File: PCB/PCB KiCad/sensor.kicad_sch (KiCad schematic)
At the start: 0 parts

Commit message: draw schematic for 60%
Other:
- note added: "TO DO: Complete analog front"
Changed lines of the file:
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@@
 (kicad_sch (version 20211123) (generator eeschema)
   (paper "A4")
+  (text "TO DO:\nComplete analog front" (at 118.11 80.01 0)
+    (effects (font (size 1.5 1.5)) (justify left bottom))
+  )
 )

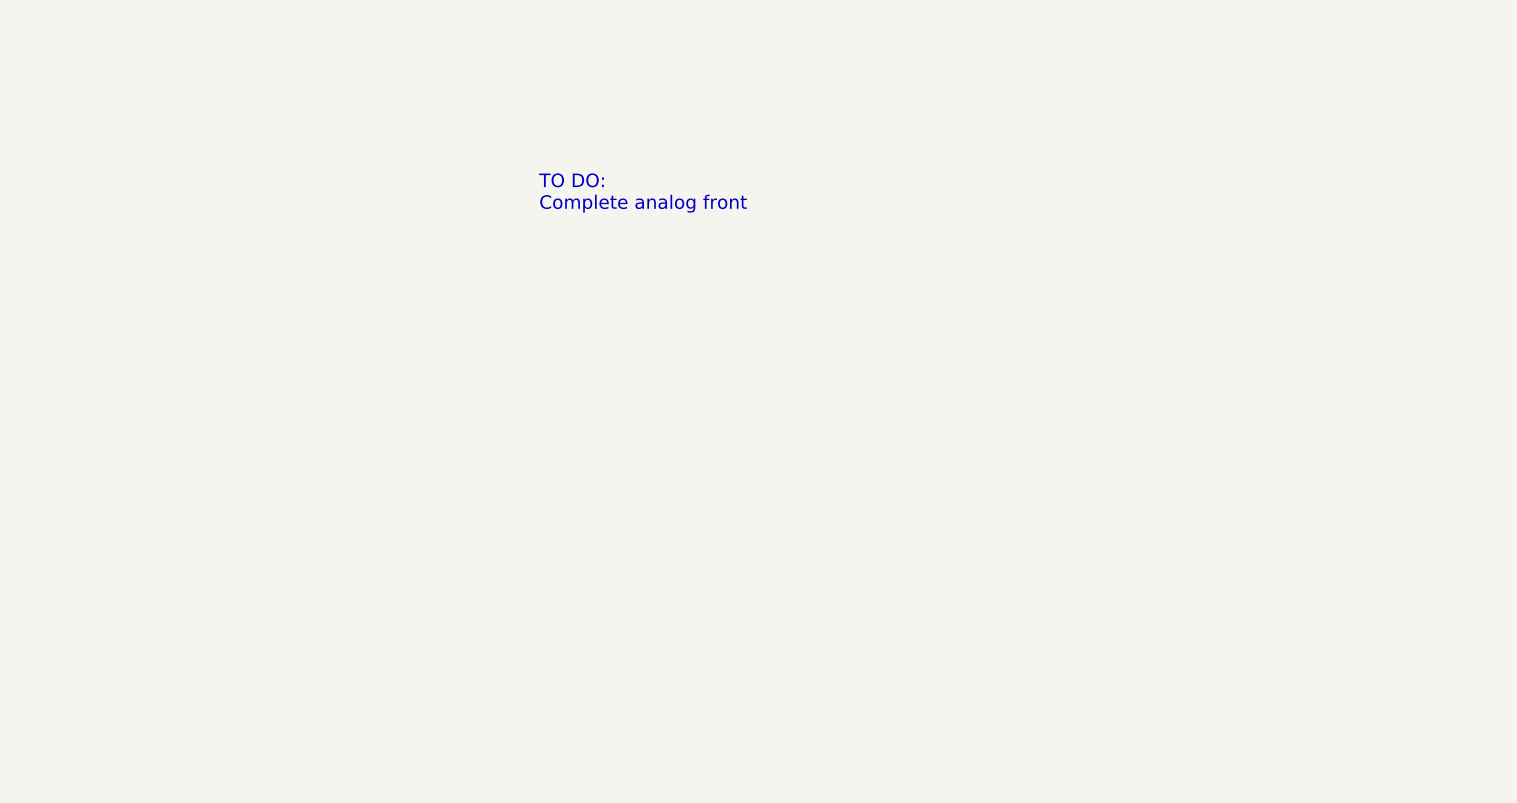
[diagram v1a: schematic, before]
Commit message: Add buttons: MCU RESET, TRIGGER
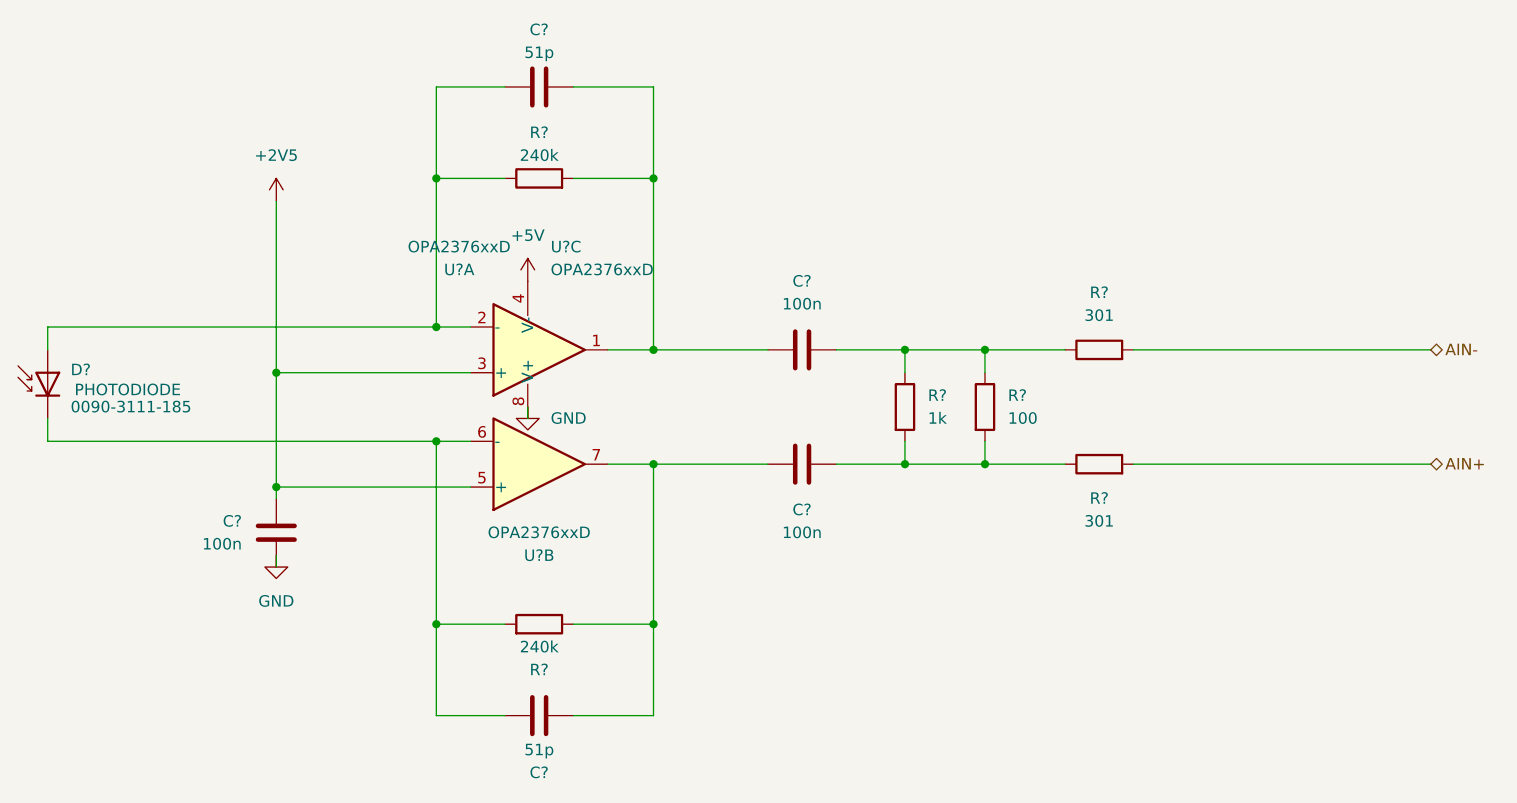
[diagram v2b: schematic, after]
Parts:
- added C? (x2): 51p, symbol Device:C
- added C? (x3): 100n, symbol Device:C
- added D?: 0090-3111-185, symbol Device:D_Photo
- added R?: 100, symbol Device:R
- added R? (x2): 240k, symbol Device:R
- added R? (x2): 301, symbol Device:R
- added R?: 1k, symbol Device:R
- added U? (x3): OPA2376xxD, symbol Amplifier_Operational:OPA2376xxD
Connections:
- new net: C?.2, R?.1, R?.1, R?.1
- new net: C?.2, R?.1, R?.2, R?.2
- new net: C?.1, C?.2, R?.1, U?.7
- new net: C?.1, D?.1 (K), R?.2, U?.6 (-)
- new net: C?.1, D?.2 (A), R?.1, U?.2 (-)
- new net: C?.1, C?.2, R?.2, U?.1
- new net +2V5: C?.2, U?.3 (+), U?.5 (+)
- new net +5V: U?.4 (V-)
- new net AIN+: R?.2
- new net AIN-: R?.2
- new net GND: C?.1, U?.8 (V+)
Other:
- note removed: "TO DO: Complete analog front"
